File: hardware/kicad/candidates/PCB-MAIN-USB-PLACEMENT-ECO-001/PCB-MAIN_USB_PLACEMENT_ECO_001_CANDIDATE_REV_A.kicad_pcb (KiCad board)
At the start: 6 copper layers, 110 x 75 mm, 251 parts, among them J10 U.FL-R-SMT-1(60), J11 USB4105-GF-A-120, J12 MEM2052-00-195-00-A, J13 504050-0291, J6 2336582-1, J7 2336582-1, J8 U.FL-R-SMT-1(60), J9 U.FL-R-SMT-1(60), Q1 MMBT3904,215, Q2 MMBT3904,215, Q3 MMBT3904,215, Q4 Si1016X-T1-GE3, U1 STM32U585VIT6Q, U10 E22-900M22S, U11 MDBT50Q-P1MV2, U13 TS3A27518EPWR, U14 ESDALC6V1-5P6, U15 ESDALC6V1-5P6, U16 SN74AXC8T245PWR, U17 SN74LVC32APWR, U18 SN74AXC1T45DRLR, U19 TPD4E05U06DQAR, U2 W25Q512JVFIQ, U20 TPD4E05U06DQAR, U21 TPD4E05U06DQAR, U22 TPD4E05U06DQAR, U23 TPD4E05U06DQAR, U24 TPD4E05U06DQAR, U25 TPD2EUSB30DRTR, U26 TPD2EUSB30DRTR, U27 TPD4E05U06DQAR, U3 LIS2DW12TR, U4 STTS22HTR, U5 LT6000IDCB#TRMPBF, U6 SN74LVC1G07DBVR, U7 SN74AXC8T245PWR, U8 BG95-M3, U9 MAX-M10S-00B, X1 SiT1552AI-JE-DCC-32.768D

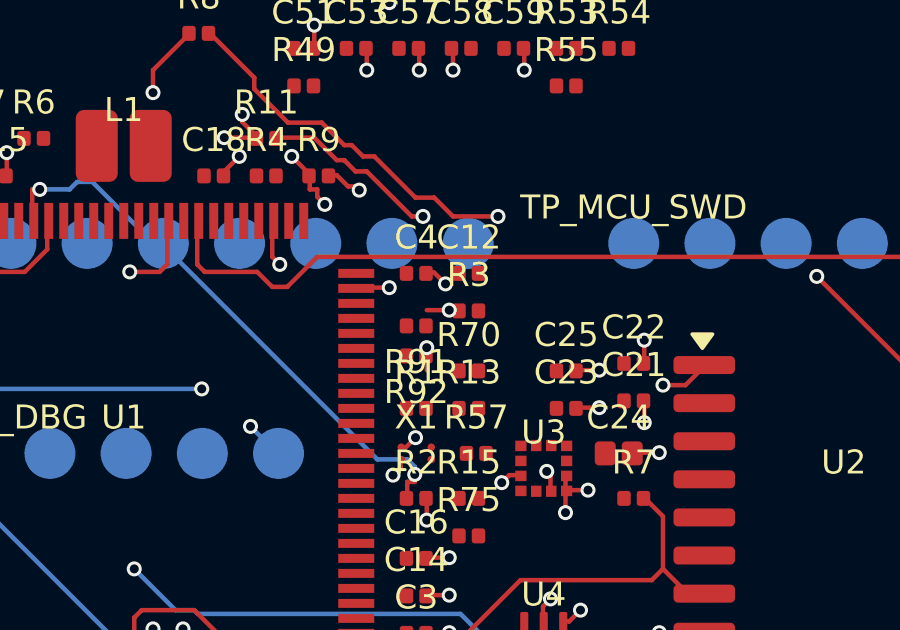
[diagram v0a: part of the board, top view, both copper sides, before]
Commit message: hardware: constrain USB placement ECO to terminations
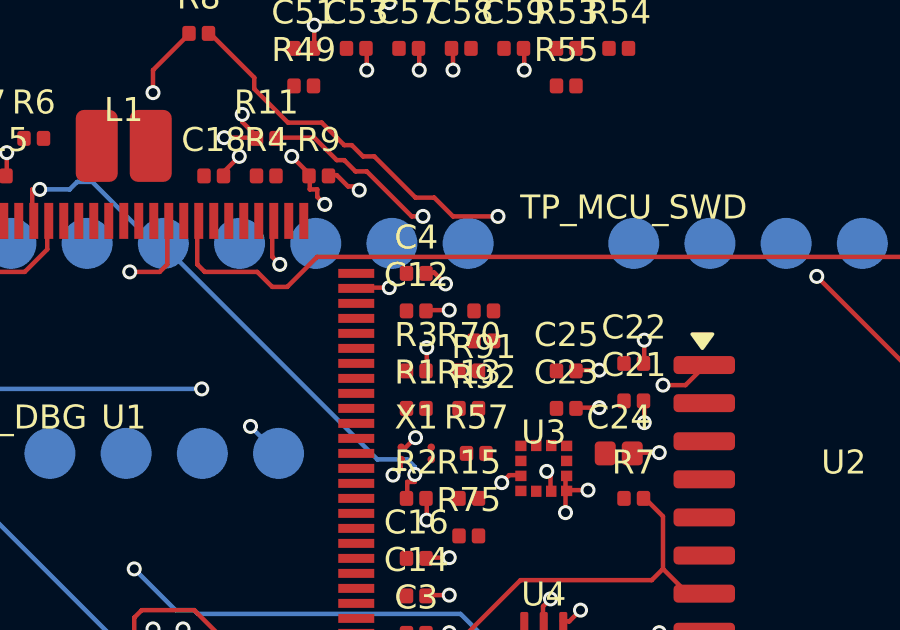
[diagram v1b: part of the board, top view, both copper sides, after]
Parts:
- moved R3 2.66 mm to (61.8, 27.2)
- moved R91 2.30 mm to (64.0, 25.2)
- moved R92 2.30 mm to (64.0, 26.2)
- moved C12 2.15 mm to (61.8, 25.2)
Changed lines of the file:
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@@
   )
   (footprint "" (layer "F.Cu")
-    (at 63.5 25.25)
+    (at 61.75 27.25)
     (property "DIONEA_COURTYARD_SOURCE" "PCB_MAIN_PASSIVE_COURTYARD_RULE_REV_A")
     (property "DIONEA_COURTYARD_STATUS" "CONTROLLED_PAD_ENVELOPE_PLUS_0.25_MM")
@@
   )
   (footprint "" (layer "F.Cu")
-    (at 61.75 26.75)
+    (at 64 26.25)
     (property "DIONEA_COURTYARD_SOURCE" "PCB_MAIN_PASSIVE_COURTYARD_RULE_REV_A")
     (property "DIONEA_COURTYARD_STATUS" "CONTROLLED_PAD_ENVELOPE_PLUS_0.25_MM")
@@
   )
   (footprint "" (layer "F.Cu")
-    (at 61.75 25.75)
+    (at 64 25.25)
     (property "DIONEA_COURTYARD_SOURCE" "PCB_MAIN_PASSIVE_COURTYARD_RULE_REV_A")
     (property "DIONEA_COURTYARD_STATUS" "CONTROLLED_PAD_ENVELOPE_PLUS_0.25_MM")
@@
   )
   (footprint "" (layer "F.Cu")
-    (at 63.5 24)
-    (property "DIONEA_COURTYARD_SOURCE" "PCB_MAIN_PASSIVE_COURTYARD_RULE_REV_A")
-    (property "DIONEA_COURTYARD_STATUS" "CONTROLLED_PAD_ENVELOPE_PLUS_0.25_MM")
+    (at 61.75 25.25)
+    (property "DIONEA_COURTYARD_SOURCE" "PCB_MAIN_PASSIVE_COURTYARD_RULE_REV_A")
+    (property "DIONEA_COURTYARD_STATUS" "CONTROLLED_PAD_ENVELOPE_PLUS_0.25_MM")
